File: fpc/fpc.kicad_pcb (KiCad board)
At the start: 2 copper layers, 40 x 19 mm, 2 parts, among them J1 usdex-fpc-cable-sd-side, J2 usdex-fpc-cable-m2-side

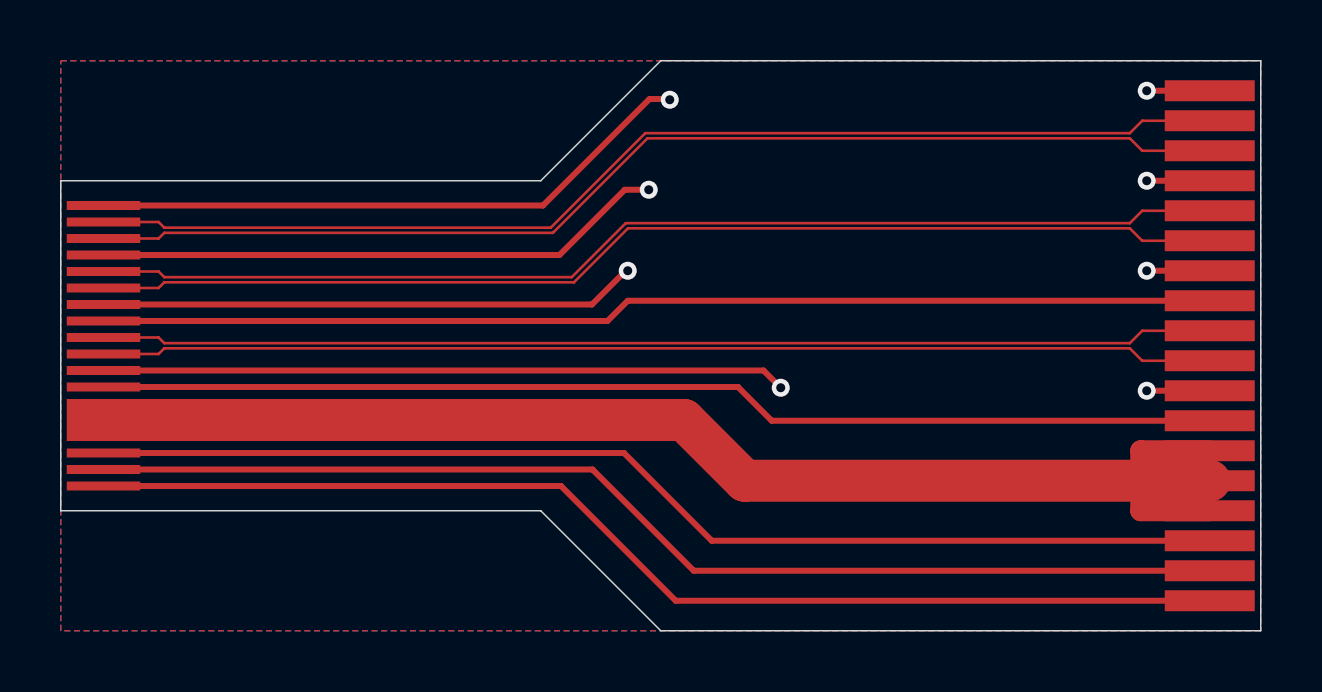
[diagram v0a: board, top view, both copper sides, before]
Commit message: add fillets and skew tuning
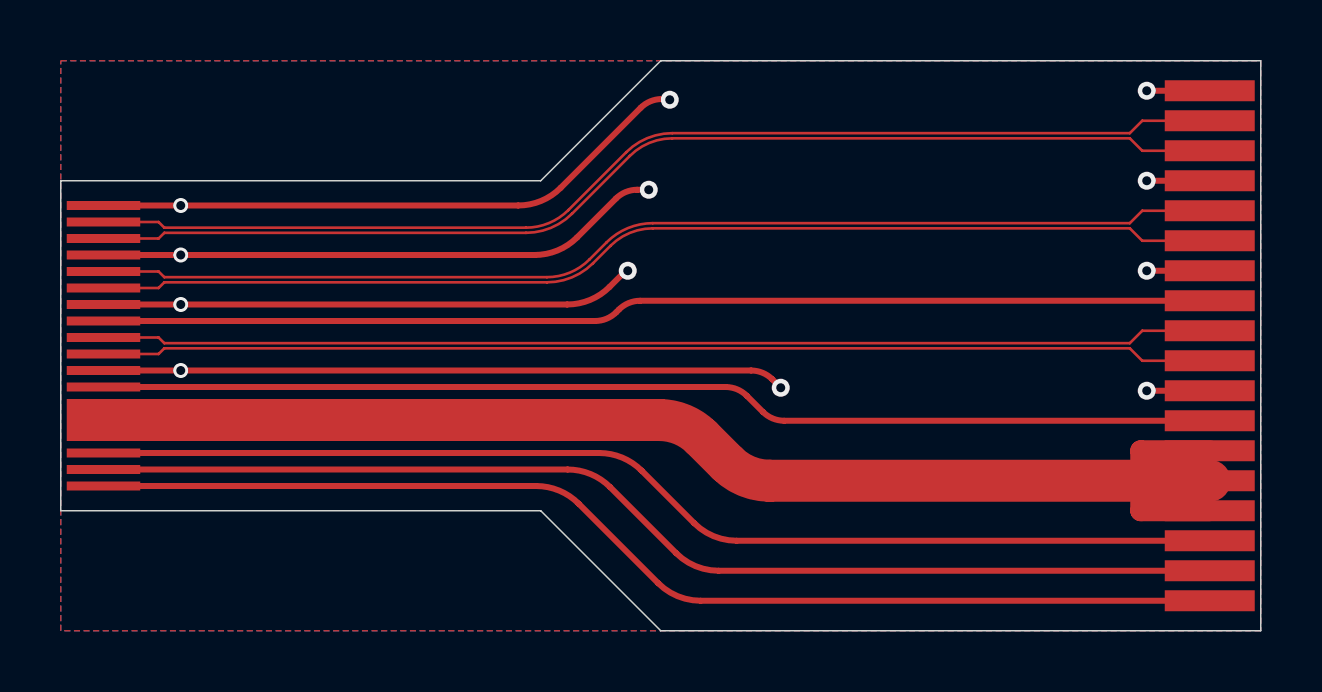
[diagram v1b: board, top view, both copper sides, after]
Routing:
- net GND: track 88.6 -> 88.2 mm, vias 8 -> 12
